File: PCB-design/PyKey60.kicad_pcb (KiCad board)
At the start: 2 copper layers, 351 x 121.5 mm, 303 parts, among them J1 USB_C_Receptacle_USB2.0, J2 Conn_01x03, SW1 SW_SPST, SW2 SW_SPDT, U1 CherryMX_LTST-A683CEGBW, U10 CherryMX_LTST-A683CEGBW, U100 RP2040, U101 USBLC6-2SC6, U102 W25Q128JVS, U103 AMS1117-3.3, U11 CherryMX_LTST-A683CEGBW, U12 CherryMX_LTST-A683CEGBW, U13 CherryMX_LTST-A683CEGBW, U14 CherryMX_LTST-A683CEGBW, U15 CherryMX_LTST-A683CEGBW, U16 CherryMX_LTST-A683CEGBW, U17 CherryMX_LTST-A683CEGBW, U18 CherryMX_LTST-A683CEGBW, U19 CherryMX_LTST-A683CEGBW, U2 CherryMX_LTST-A683CEGBW, U20 CherryMX_LTST-A683CEGBW, U21 CherryMX_LTST-A683CEGBW, U22 CherryMX_LTST-A683CEGBW, U23 CherryMX_LTST-A683CEGBW, U24 CherryMX_LTST-A683CEGBW, U25 CherryMX_LTST-A683CEGBW, U26 CherryMX_LTST-A683CEGBW, U27 CherryMX_LTST-A683CEGBW, U28 CherryMX_LTST-A683CEGBW, U29 CherryMX_LTST-A683CEGBW, U3 CherryMX_LTST-A683CEGBW, U30 CherryMX_LTST-A683CEGBW, U31 CherryMX_LTST-A683CEGBW, U32 CherryMX_LTST-A683CEGBW, U33 CherryMX_LTST-A683CEGBW, U34 CherryMX_LTST-A683CEGBW, U35 CherryMX_LTST-A683CEGBW, U36 CherryMX_LTST-A683CEGBW, U37 CherryMX_LTST-A683CEGBW, U38 CherryMX_LTST-A683CEGBW, U39 CherryMX_LTST-A683CEGBW, U4 CherryMX_LTST-A683CEGBW, U40 CherryMX_LTST-A683CEGBW, U41 CherryMX_LTST-A683CEGBW, U42 CherryMX_LTST-A683CEGBW, U43 CherryMX_LTST-A683CEGBW, U44 CherryMX_LTST-A683CEGBW, U45 CherryMX_LTST-A683CEGBW, U46 CherryMX_LTST-A683CEGBW, U47 CherryMX_LTST-A683CEGBW, U48 CherryMX_LTST-A683CEGBW, U49 CherryMX_LTST-A683CEGBW, U5 CherryMX_LTST-A683CEGBW, U50 CherryMX_LTST-A683CEGBW, U51 CherryMX_LTST-A683CEGBW, U52 CherryMX_LTST-A683CEGBW, U53 CherryMX_LTST-A683CEGBW, U54 CherryMX_LTST-A683CEGBW, U55 CherryMX_LTST-A683CEGBW, U56 CherryMX_LTST-A683CEGBW, U57 CherryMX_LTST-A683CEGBW, U58 CherryMX_LTST-A683CEGBW, U59 CherryMX_LTST-A683CEGBW, U6 CherryMX_LTST-A683CEGBW, U60 CherryMX_LTST-A683CEGBW, U61 CherryMX_LTST-A683CEGBW, U62 CherryMX_LTST-A683CEGBW, U63 CherryMX_LTST-A683CEGBW, U64 CherryMX_LTST-A683CEGBW, U65 CherryMX_LTST-A683CEGBW, U66 CherryMX_LTST-A683CEGBW, U67 CherryMX_LTST-A683CEGBW, U68 CherryMX_LTST-A683CEGBW, U69 CherryMX_LTST-A683CEGBW, U7 CherryMX_LTST-A683CEGBW, U70 CherryMX_LTST-A683CEGBW, U71 CherryMX_LTST-A683CEGBW, U72 CherryMX_LTST-A683CEGBW, U73 CherryMX_LTST-A683CEGBW, U74 CherryMX_LTST-A683CEGBW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

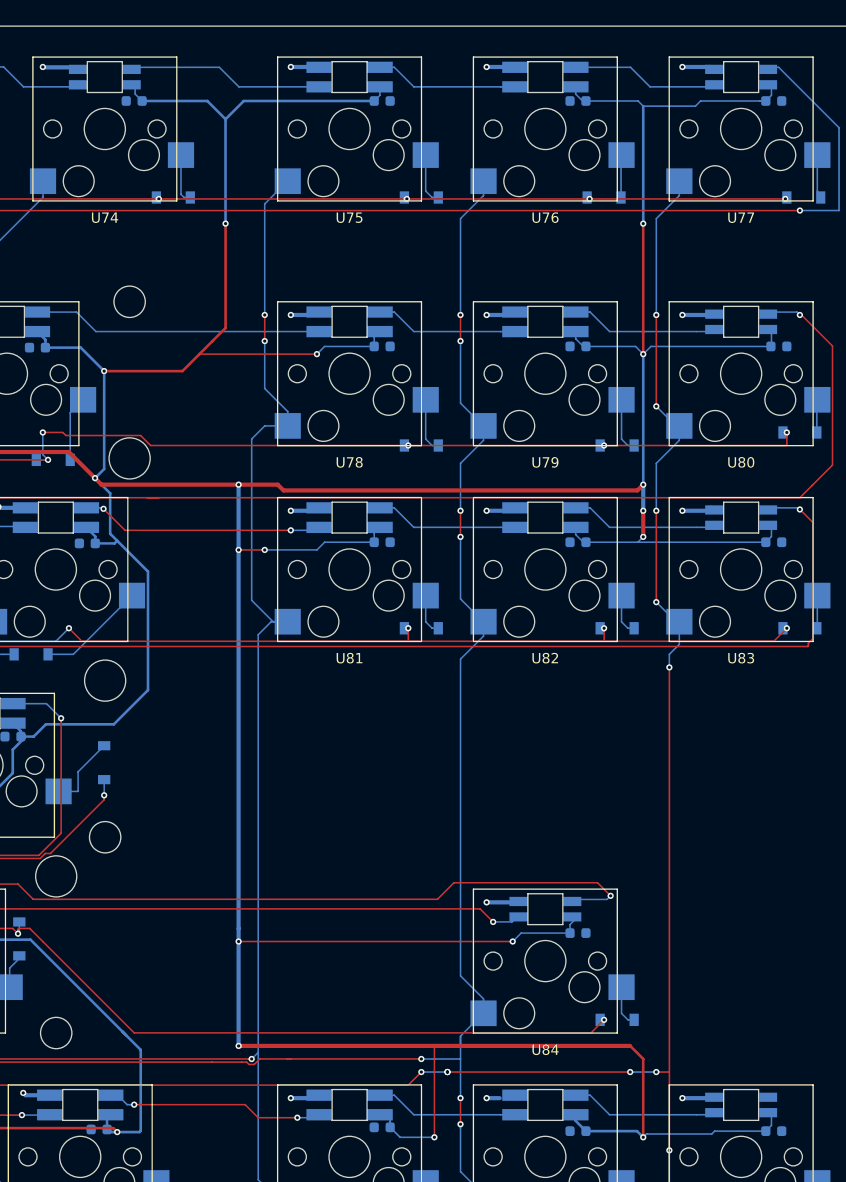
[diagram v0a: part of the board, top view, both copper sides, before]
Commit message: Fix Footprints and Cap Names
Renamed capacitors to correspond with keys (non-key caps shifted +87). Fixed rogue footprints to rotated hand-solder versions.
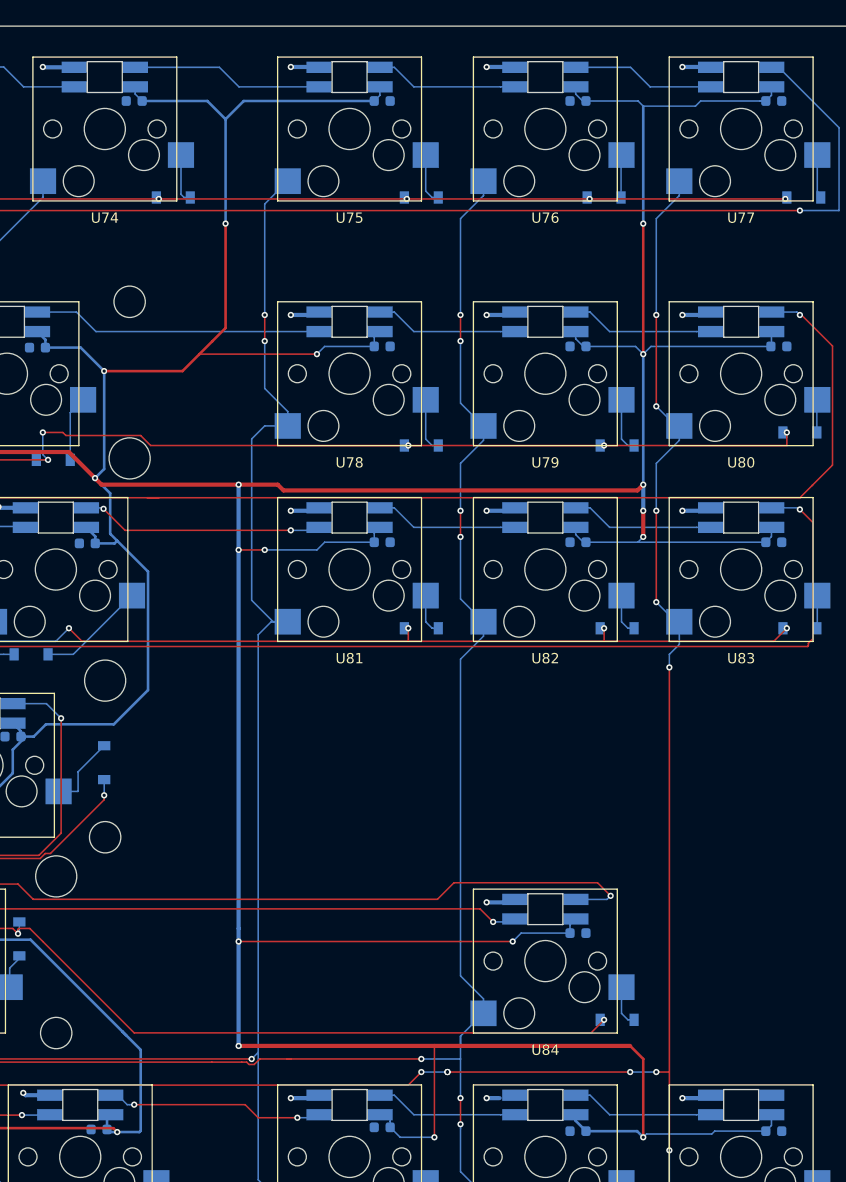
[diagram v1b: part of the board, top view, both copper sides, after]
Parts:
- U74, U77, U80, U83, U84, U87: footprint CherryMX_PCB_KailhSocket_LTST-A683CEGBW-Rotated:CherryMX_1.00u_PCB_KailhSocket_LTST-A683CEGBW-Rotated -> CherryMX_PCB_KailhSocket_LTST-A683CEGBW-Rotated-HS:CherryMX_1.00u_PCB_KailhSocket_LTST-A683CEGBW-Rotated-HS
- renumbered C41 to C1, C72 to C10, C13 to C100, C14 to C101, C15 to C102, C16 to C103, C74 to C11, C69 to C12, C64 to C13, C71 to C14, C77 to C15, C26 to C16, C46 to C17, C54 to C18, C63 to C19, C47 to C2, C60 to C20, C68 to C21, C70 to C22, C76 to C23, C75 to C24, C52 to C25, C44 to C26, C38 to C27, C25 to C28, C40 to C29, C62 to C3, C21 to C30, C18 to C31, C61 to C32, C53 to C33, C67 to C34, C73 to C35, C66 to C36, C59 to C37, C58 to C38, C35 to C39, C55 to C4, C19 to C40, C29 to C41, C24 to C41, C30 to C43, C37 to C44, C48 to C45, C45 to C46, C56 to C47, C51 to C48, C50 to C49, C39 to C5, C43 to C50, C34 to C51, C22 to C52, C36 to C53, C20 to C54, C32 to C55, C17 to C56, C42 to C57, C28 to C58, C27 to C59, C33 to C6, C23 to C60, C31 to C61, C65 to C62, C65 to C63, C65 to C64, C65 to C66, C65 to C67, C65 to C68, C65 to C69, C49 to C7, C65 to C70, C65 to C71, C65 to C72, C65 to C73, C65 to C74, C65 to C75, C65 to C76, C65 to C77, C65 to C78, C65 to C79, C57 to C8, C65 to C80, C65 to C81, C65 to C82, C65 to C83, C65 to C84, C65 to C85, C65 to C86, C65 to C87, C1 to C88, C2 to C89, C65 to C9, C3 to C90, C4 to C91, C5 to C92, C6 to C93, C7 to C94, C8 to C95, C9 to C96, C10 to C97, C11 to C98, C12 to C99

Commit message: Add new mounting holes
Also shift some traces to make it work
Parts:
- removed H1: MountingHole, lib.pretty:PKRHC
- removed H2, H4, H6: MountingHole, lib.pretty:PKRH
- removed H3, H5: MountingHole, lib.pretty:PKRHSL
- added REF**: MountingHole_2.7mm_M2.5_Pad, MountingHole:MountingHole_2.7mm_M2.5_Pad, F.Cu at (402.5, 61.8)
- added REF**: MountingHole_2.7mm_M2.5_Pad, MountingHole:MountingHole_2.7mm_M2.5_Pad, F.Cu at (402.5, 132.9)
- added REF**: MountingHole_2.7mm_M2.5_Pad, MountingHole:MountingHole_2.7mm_M2.5_Pad, F.Cu at (233.0, 61.8)
- added REF**: MountingHole_2.7mm_M2.5_Pad, MountingHole:MountingHole_2.7mm_M2.5_Pad, F.Cu at (233.0, 151.9)
- added REF**: MountingHole_2.7mm_M2.5_Pad, MountingHole:MountingHole_2.7mm_M2.5_Pad, F.Cu at (65.4, 61.8)
- added REF**: MountingHole_2.7mm_M2.5_Pad, MountingHole:MountingHole_2.7mm_M2.5_Pad, F.Cu at (65.4, 132.9)
- moved LS1 2.54 mm to (217.8, 151.9)
- moved J1 1.50 mm to (88.4, 44.0)
- moved R1 0.34 mm to (79.4, 41.4)
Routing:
- net RGBData1: track 382.2 -> 375.2 mm
- net ROW0: track 542.7 -> 536.0 mm
- net COL1: track 210.3 -> 213.7 mm
- net VBUS: track 107.0 -> 110.3 mm
- net Net-(U62-Pad5): track 35.7 -> 33.0 mm
- net RGBData5: track 349.2 -> 351.7 mm
- net Speaker: track 54.0 -> 52.9 mm
- net Net-(J1-PadA5): track 12.2 -> 13.2 mm
- net RGBData0: track 203.7 -> 204.7 mm
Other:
- board size 351 x 121.5 mm -> 353 x 120 mm

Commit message: Reroute and round PCB
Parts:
- renumbered REF** to H1, REF** to H2, REF** to H3, REF** to H4, REF** to H5, REF** to H6
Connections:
- U100 pad 32: COL17 -> Speaker
- U100 pad 34: Speaker -> (no net)
- U100 pad 35: Net-(U100-Pad35) -> (no net)
- U100 pad 36: ROW0 -> LED
- U100 pad 37: Net-(U100-Pad37) -> COL17
- U100 pad 38: Net-(U100-Pad38) -> (no net)
- U100 pad 39: LED -> ROW0
- U100 pad 40: Net-(U100-Pad40) -> (no net)
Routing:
- net LED: track 140.7 -> 143.2 mm
- net COL17: track 346.4 -> 348.0 mm, vias 14 -> 16
- net Speaker: track 52.9 -> 51.7 mm
- net /RESET: track 110.1 -> 110.6 mm
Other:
- outline, holes or cut-outs redrawn
